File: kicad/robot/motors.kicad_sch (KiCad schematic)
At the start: 20 parts, among them J3 Conn_01x06_MountingPin, J5 Conn_01x06_MountingPin, Q6 SN74AHC125RGYR, U8 DRV8830DRCR, U9 DRV8830DRCR

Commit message: Exported all schematic symbols to local robot and refer to them in all symbols
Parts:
- C40, C41, C42, C43, C44, C74: symbol Device:C -> robot:C
- J3, J5: symbol Connector_Generic_MountingPin:Conn_01x06_MountingPin -> robot:Conn_01x06_MountingPin
- Q6: symbol ultralibrarian:SN74AHC125RGYR -> robot:SN74AHC125RGYR
- R26, R27, R28, R29, R30, R31: symbol Device:R -> robot:R
- U8, U9: symbol Driver_Motor:DRV8830DRCR -> robot:DRV8830DRCR
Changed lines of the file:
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@@
     (effects (font (size 1.27 1.27)) (justify right))
   )
-  (symbol (lib_id "ultralibrarian:SN74AHC125RGYR") (at 218.44 160.02 0) (unit 1)
+  (symbol (lib_id "robot:SN74AHC125RGYR") (at 218.44 160.02 0) (unit 1)
     (in_bom yes) (on_board yes) (dnp no) (fields_autoplaced)
     (property "Reference" "Q6" (at 221.7294 135.89 0)
@@
     )
   )
-  (symbol (lib_id "Connector_Generic_MountingPin:Conn_01x06_MountingPin") (at 245.11 52.07 0) (mirror y) (unit 1)
+  (symbol (lib_id "robot:Conn_01x06_MountingPin") (at 245.11 52.07 0) (mirror y) (unit 1)
     (in_bom yes) (on_board yes) (dnp no) (fields_autoplaced)
     (property "Reference" "J3" (at 242.57 52.4256 0)
@@
     )
   )
-  (symbol (lib_id "Device:R") (at 59.69 140.97 0) (unit 1)
+  (symbol (lib_id "robot:R") (at 59.69 140.97 0) (unit 1)
     (in_bom no) (on_board yes) (dnp yes) (fields_autoplaced)
     (property "Reference" "R27" (at 62.23 139.6999 0)
@@
     )
   )
-  (symbol (lib_id "Device:C") (at 160.02 120.65 0) (mirror y) (unit 1)
+  (symbol (lib_id "robot:C") (at 160.02 120.65 0) (mirror y) (unit 1)
     (in_bom no) (on_board yes) (dnp yes)
     (property "Reference" "C74" (at 156.21 118.1099 0)
@@
     )
   )
-  (symbol (lib_id "Device:C") (at 160.02 49.53 0) (mirror y) (unit 1)
+  (symbol (lib_id "robot:C") (at 160.02 49.53 0) (mirror y) (unit 1)
     (in_bom no) (on_board yes) (dnp yes)
     (property "Reference" "C74" (at 156.21 46.9899 0)
@@
     )
   )
-  (symbol (lib_id "Connector_Generic_MountingPin:Conn_01x06_MountingPin") (at 232.41 52.07 0) (unit 1)
+  (symbol (lib_id "robot:Conn_01x06_MountingPin") (at 232.41 52.07 0) (unit 1)
     (in_bom yes) (on_board yes) (dnp no) (fields_autoplaced)
     (property "Reference" "J5" (at 234.95 52.4256 0)
@@
     )
   )
-  (symbol (lib_id "Device:C") (at 130.81 49.53 0) (unit 1)
+  (symbol (lib_id "robot:C") (at 130.81 49.53 0) (unit 1)
     (in_bom yes) (on_board yes) (dnp no)
     (property "Reference" "C42" (at 134.62 48.2599 0)
@@
     )
   )
-  (symbol (lib_id "Device:R") (at 67.31 41.91 0) (unit 1)
+  (symbol (lib_id "robot:R") (at 67.31 41.91 0) (unit 1)
     (in_bom yes) (on_board yes) (dnp no) (fields_autoplaced)
     (property "Reference" "R28" (at 69.85 40.6399 0)
@@
     )
   )
-  (symbol (lib_id "Device:C") (at 118.11 49.53 0) (unit 1)
+  (symbol (lib_id "robot:C") (at 118.11 49.53 0) (unit 1)
     (in_bom yes) (on_board yes) (dnp no)
     (property "Reference" "C40" (at 121.92 48.2599 0)
@@
     )
   )
-  (symbol (lib_id "Device:R") (at 59.69 69.85 0) (unit 1)
+  (symbol (lib_id "robot:R") (at 59.69 69.85 0) (unit 1)
     (in_bom no) (on_board yes) (dnp yes) (fields_autoplaced)
     (property "Reference" "R26" (at 62.23 68.5799 0)
@@
     )
   )
-  (symbol (lib_id "Device:R") (at 73.66 111.76 0) (unit 1)
+  (symbol (lib_id "robot:R") (at 73.66 111.76 0) (unit 1)
     (in_bom yes) (on_board yes) (dnp no) (fields_autoplaced)
     (property "Reference" "R31" (at 76.2 110.4899 0)
@@
     )
   )
-  (symbol (lib_id "Device:R") (at 68.58 140.97 0) (unit 1)
+  (symbol (lib_id "robot:R") (at 68.58 140.97 0) (unit 1)
     (in_bom yes) (on_board yes) (dnp no) (fields_autoplaced)
     (property "Reference" "R30" (at 70.358 140.1353 0)
@@
     )
   )
-  (symbol (lib_id "Device:C") (at 148.59 120.65 0) (mirror y) (unit 1)
+  (symbol (lib_id "robot:C") (at 148.59 120.65 0) (mirror y) (unit 1)
     (in_bom no) (on_board yes) (dnp yes)
     (property "Reference" "C74" (at 144.78 118.1099 0)
@@
     )
   )
-  (symbol (lib_id "Device:C") (at 130.81 120.65 0) (unit 1)
+  (symbol (lib_id "robot:C") (at 130.81 120.65 0) (unit 1)
     (in_bom yes) (on_board yes) (dnp no)
     (property "Reference" "C43" (at 134.62 119.3799 0)
@@
     )
   )
-  (symbol (lib_id "Driver_Motor:DRV8830DRCR") (at 96.52 129.54 0) (unit 1)
+  (symbol (lib_id "robot:DRV8830DRCR") (at 96.52 129.54 0) (unit 1)
     (in_bom yes) (on_board yes) (dnp no) (fields_autoplaced)
     (property "Reference" "U9" (at 96.52 109.22 0)
@@
     )
   )
-  (symbol (lib_id "Device:C") (at 118.11 120.65 0) (unit 1)
+  (symbol (lib_id "robot:C") (at 118.11 120.65 0) (unit 1)
     (in_bom yes) (on_board yes) (dnp no)
     (property "Reference" "C41" (at 121.92 119.3799 0)
@@
     )
   )
-  (symbol (lib_id "Driver_Motor:DRV8830DRCR") (at 96.52 58.42 0) (unit 1)
+  (symbol (lib_id "robot:DRV8830DRCR") (at 96.52 58.42 0) (unit 1)
     (in_bom yes) (on_board yes) (dnp no) (fields_autoplaced)
     (property "Reference" "U8" (at 96.52 38.1 0)
@@
     )
   )
-  (symbol (lib_id "Device:C") (at 251.46 161.29 0) (unit 1)
+  (symbol (lib_id "robot:C") (at 251.46 161.29 0) (unit 1)
     (in_bom yes) (on_board yes) (dnp no)
     (property "Reference" "C44" (at 255.27 160.0199 0)
@@
     )
   )
-  (symbol (lib_id "Device:R") (at 68.58 69.85 0) (unit 1)
+  (symbol (lib_id "robot:R") (at 68.58 69.85 0) (unit 1)
     (in_bom yes) (on_board yes) (dnp no) (fields_autoplaced)
     (property "Reference" "R29" (at 70.358 69.0153 0)
@@
     )
   )
-  (symbol (lib_id "Device:C") (at 148.59 49.53 0) (mirror y) (unit 1)
+  (symbol (lib_id "robot:C") (at 148.59 49.53 0) (mirror y) (unit 1)
     (in_bom no) (on_board yes) (dnp yes)
     (property "Reference" "C74" (at 144.78 46.9899 0)

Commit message: Removing a bunch of unneccesary symbol properties
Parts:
- Q6: Stock 50 -> (none)
- U8, U9: MAXIMUM_PACKAGE_HEIGHT 1.0mm -> (none); PARTREV G -> (none); STANDARD Manufacturer Recommendations -> (none); Stock 30 -> (none)
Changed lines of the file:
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@@
-      (effects (font (size 1.27 1.27)) hide)
-    )
-    (property "Stock" "50" (at 218.44 160.02 0)
       (effects (font (size 1.27 1.27)) hide)
     )
@@
       (effects (font (size 1.27 1.27)) (justify left bottom) hide)
     )
-    (property "MAXIMUM_PACKAGE_HEIGHT" "1.0mm" (at 83.82 157.48 0)
-      (effects (font (size 1.27 1.27)) (justify left bottom) hide)
-    )
-    (property "STANDARD" "Manufacturer Recommendations" (at 83.82 154.94 0)
-      (effects (font (size 1.27 1.27)) (justify left bottom) hide)
-    )
-    (property "MANUFACTURER" "" (at 83.82 152.4 0)
-      (effects (font (size 1.27 1.27)) (justify left bottom) hide)
-    )
-    (property "PARTREV" "G" (at 83.82 160.02 0)
-      (effects (font (size 1.27 1.27)) (justify left bottom) hide)
-    )
     (property "Description" "Provide adequate heat sinking on PCB" (at 96.52 129.54 0)
       (effects (font (size 1.27 1.27)) hide)
@@
     )
     (property "Part Number" "DRV8830DRCR" (at 96.52 129.54 0)
-      (effects (font (size 1.27 1.27)) hide)
-    )
-    (property "Stock" "30" (at 96.52 129.54 0)
       (effects (font (size 1.27 1.27)) hide)
     )
@@
       (effects (font (size 1.27 1.27)) (justify left bottom) hide)
     )
-    (property "MAXIMUM_PACKAGE_HEIGHT" "1.0mm" (at 83.82 86.36 0)
-      (effects (font (size 1.27 1.27)) (justify left bottom) hide)
-    )
-    (property "STANDARD" "Manufacturer Recommendations" (at 83.82 83.82 0)
-      (effects (font (size 1.27 1.27)) (justify left bottom) hide)
-    )
-    (property "MANUFACTURER" "" (at 83.82 81.28 0)
-      (effects (font (size 1.27 1.27)) (justify left bottom) hide)
-    )
-    (property "PARTREV" "G" (at 83.82 88.9 0)
-      (effects (font (size 1.27 1.27)) (justify left bottom) hide)
-    )
     (property "Description" "Provide adequate heat sinking on PCB" (at 96.52 58.42 0)
       (effects (font (size 1.27 1.27)) hide)
@@
       (effects (font (size 1.27 1.27)) hide)
     )
-    (property "Stock" "30" (at 96.52 58.42 0)
-      (effects (font (size 1.27 1.27)) hide)
-    )

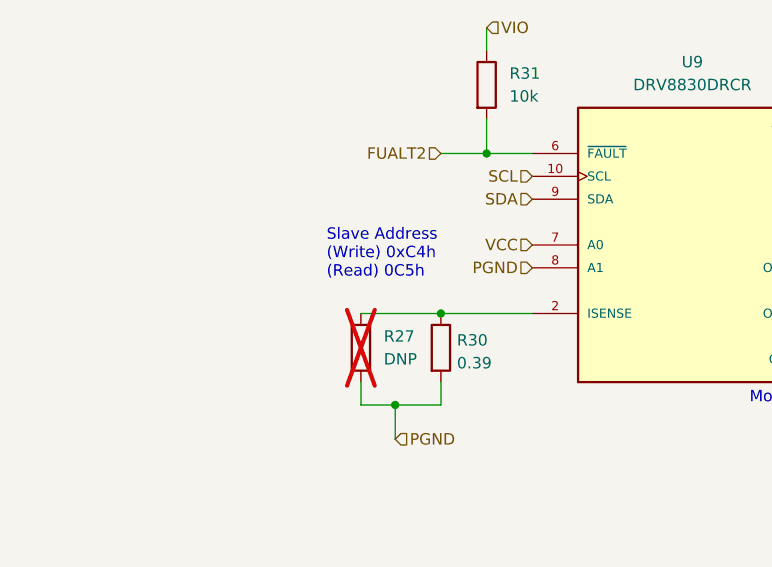
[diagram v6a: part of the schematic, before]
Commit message: Added power_2A net classes and net ties to schematic
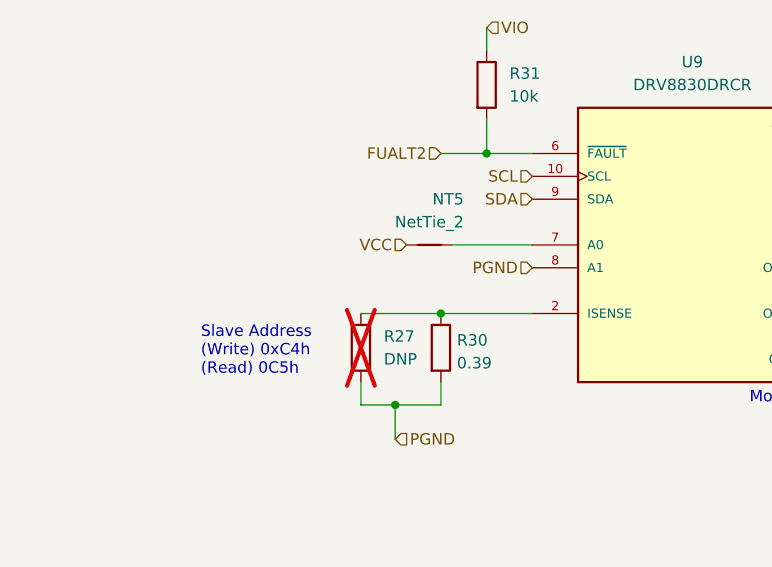
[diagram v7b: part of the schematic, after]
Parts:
- added NT5: NetTie_2, robot:NetTie-_SMD_Pad6mil, symbol Device:NetTie_2
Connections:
- net VCC: now also NT5.2; no longer U9.7 (A0)
- new net: NT5.1, U9.7 (A0)
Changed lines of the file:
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@@
+    (stroke (width 0) (type default))
+  )
+  (wire (pts (xy 69.85 129.54) (xy 78.74 129.54))
     (stroke (width 0) (type default))
   )
@@
     (effects (font (size 1.27 1.27)) (justify left bottom))
   )
-  (text "Slave Address \n(Write) 0xC4h \n(Read) 0C5h" (at 55.88 133.35 0)
+  (text "Slave Address \n(Write) 0xC4h \n(Read) 0C5h" (at 41.91 144.145 0)
     (effects (font (size 1.27 1.27)) (justify left bottom))
   )
@@
     (effects (font (size 1.27 1.27)) (justify left))
   )
-  (hierarchical_label "VCC" (shape input) (at 78.74 129.54 180) (fields_autoplaced)
+  (hierarchical_label "VCC" (shape input) (at 64.77 129.54 180) (fields_autoplaced)
     (effects (font (size 1.27 1.27)) (justify right))
   )
@@
   (hierarchical_label "PGND" (shape input) (at 78.74 132.08 180) (fields_autoplaced)
     (effects (font (size 1.27 1.27)) (justify right))
+  )
+  (netclass_flag "" (length 2.54) (shape round) (at 115.57 66.04 0) (fields_autoplaced)
+    (effects (font (size 1.27 1.27)) (justify left bottom))
+    (property "Netclass" "power_2A" (at 116.2685 63.5 0)
+      (effects (font (size 1.27 1.27) italic) (justify left) hide)
+    )
+  )
+  (netclass_flag "" (length 2.54) (shape round) (at 115.57 60.96 0) (fields_autoplaced)
+    (effects (font (size 1.27 1.27)) (justify left bottom))
+    (property "Netclass" "power_2A" (at 116.2685 58.42 0)
+      (effects (font (size 1.27 1.27) italic) (justify left) hide)
+    )
+  )
+  (netclass_flag "" (length 2.54) (shape round) (at 114.935 132.08 0) (fields_autoplaced)
+    (effects (font (size 1.27 1.27)) (justify left bottom))
+    (property "Netclass" "power_2A" (at 115.6335 129.54 0)
+      (effects (font (size 1.27 1.27) italic) (justify left) hide)
+    )
+  )
+  (netclass_flag "" (length 2.54) (shape round) (at 114.935 137.16 0) (fields_autoplaced)
+    (effects (font (size 1.27 1.27)) (justify left bottom))
+    (property "Netclass" "power_2A" (at 115.6335 134.62 0)
+      (effects (font (size 1.27 1.27) italic) (justify left) hide)
+    )
   )
   (symbol (lib_id "robot:SN74AHC125RGYR") (at 218.44 160.02 0) (unit 1)
@@
         )
       )
+    )
+  )
+  (symbol (lib_id "Device:NetTie_2") (at 67.31 129.54 0) (mirror y) (unit 1)
+    (in_bom no) (on_board yes) (dnp no)
+    (property "Reference" "NT5" (at 71.12 124.46 0)
+      (effects (font (size 1.27 1.27)) (justify left))
+    )
+    (property "Value" "NetTie_2" (at 71.12 127 0)
+      (effects (font (size 1.27 1.27)) (justify left))
+    )
+    (property "Footprint" "robot:NetTie-_SMD_Pad6mil" (at 67.31 129.54 0)
+      (effects (font (size 1.27 1.27)) hide)
+    )
+    (property "Datasheet" "~" (at 67.31 129.54 0)
+      (effects (font (size 1.27 1.27)) hide)
+    )
+    (pin "1")
+    (pin "2")
+    (instances
+      (project "robot"
+        (path "/0c7b298e-2d07-4b1f-b033-e95f02d45089/3fab603d-ed65-41bd-8de1-51639e39cb06"
+          (reference "NT5") (unit 1)
+        )
+        (path "/0c7b298e-2d07-4b1f-b033-e95f02d45089/aaf20b87-68dc-43c9-a7d3-4ceda8b87424"
+          (reference "NT15") (unit 1)
+        )
+        (path "/0c7b298e-2d07-4b1f-b033-e95f02d45089/427922e5-a943-4728-8788-709c0c3b2395"
+          (reference "NT16") (unit 1)
+        )
+        (path "/0c7b298e-2d07-4b1f-b033-e95f02d45089/4bf796fd-fdb4-45d1-808a-a634d5f4571e"
+          (reference "NT17") (unit 1)
+        )
+      )

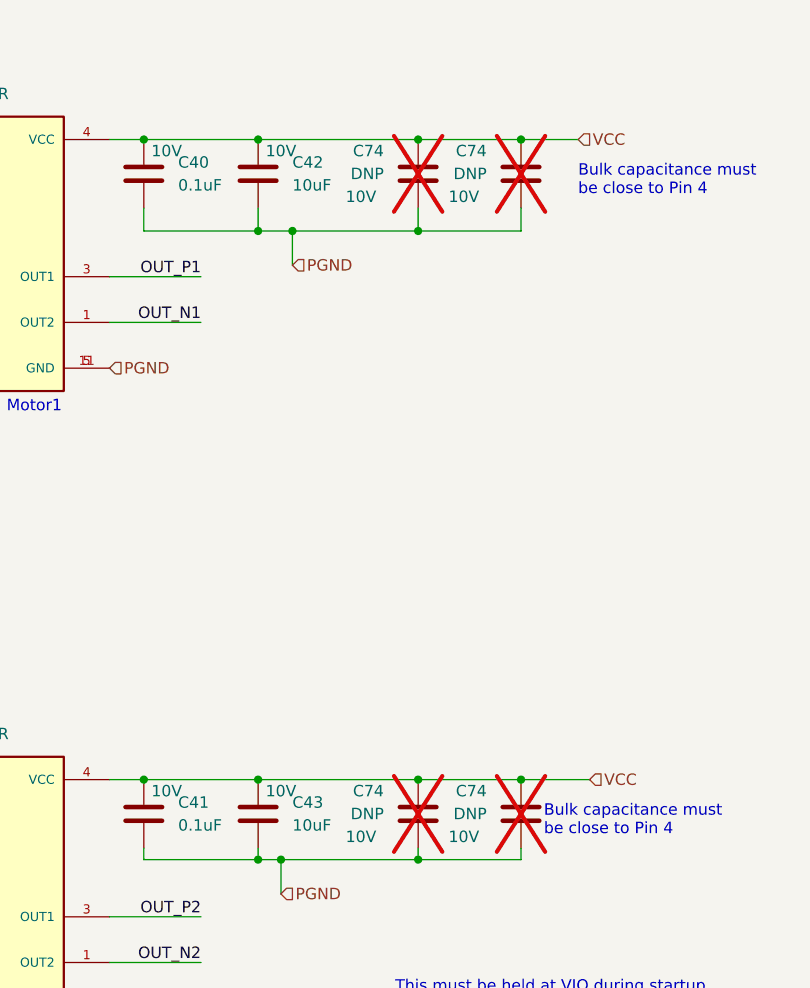
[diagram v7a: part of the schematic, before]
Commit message: Updating symbol fields for BOM completion.
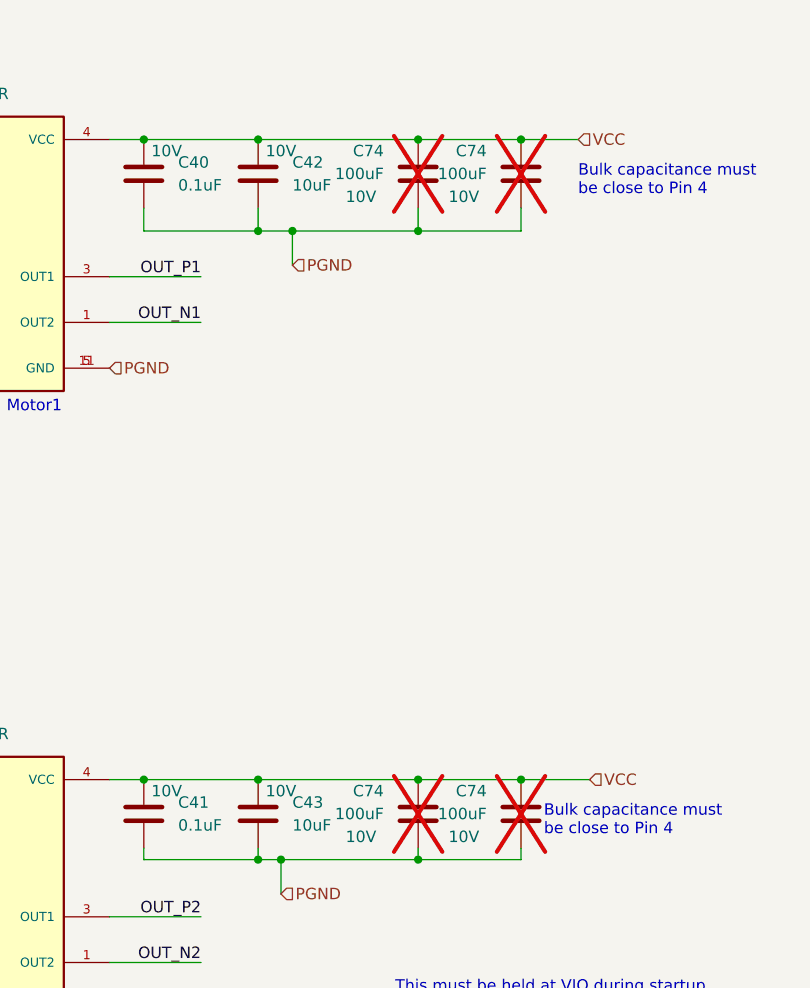
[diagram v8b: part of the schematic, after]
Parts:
- C74: value DNP -> 100uF; Manufacturer DNP -> Murata; Part Number DNP -> GRM31CD80J107MEA8K
- J3, J5: Manufacturer (none) -> JST; Part Number (none) -> B6B-ZR-SM4-TF
- NT5: Manufacturer (none) -> N/A; Part Number (none) -> N/A
- R26, R27: Manufacturer DNP -> Panasonic; Part Number DNP -> ERJ-3RQJR39V
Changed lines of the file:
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@@
+      (effects (font (size 1.27 1.27)) hide)
+    )
+    (property "Manufacturer" "N/A" (at 67.31 129.54 0)
+      (effects (font (size 1.27 1.27)) hide)
+    )
+    (property "Part Number" "N/A" (at 67.31 129.54 0)
       (effects (font (size 1.27 1.27)) hide)
     )
@@
     )
     (property "Datasheet" "https://www.jst-mfg.com/product/pdf/eng/eZH.pdf" (at 245.11 52.07 0)
+      (effects (font (size 1.27 1.27)) hide)
+    )
+    (property "Manufacturer" "JST" (at 245.11 52.07 0)
+      (effects (font (size 1.27 1.27)) hide)
+    )
+    (property "Part Number" "B6B-ZR-SM4-TF" (at 245.11 52.07 0)
       (effects (font (size 1.27 1.27)) hide)
     )
@@
       (effects (font (size 1.27 1.27)) hide)
     )
-    (property "Manufacturer" "DNP" (at 59.69 140.97 0)
-      (effects (font (size 1.27 1.27)) hide)
-    )
-    (property "Part Number" "DNP" (at 59.69 140.97 0)
+    (property "Manufacturer" "Panasonic" (at 59.69 140.97 0)
+      (effects (font (size 1.27 1.27)) hide)
+    )
+    (property "Part Number" "ERJ-3RQJR39V" (at 59.69 140.97 0)
       (effects (font (size 1.27 1.27)) hide)
     )
@@
       (effects (font (size 1.27 1.27)) (justify left))
     )
-    (property "Value" "DNP" (at 156.21 120.6499 0)
+    (property "Value" "100uF" (at 156.21 120.6499 0)
       (effects (font (size 1.27 1.27)) (justify left))
     )
@@
       (effects (font (size 1.27 1.27)))
     )
-    (property "Manufacturer" "DNP" (at 160.02 120.65 0)
-      (effects (font (size 1.27 1.27)) hide)
-    )
-    (property "Part Number" "DNP" (at 160.02 120.65 0)
+    (property "Manufacturer" "Murata" (at 160.02 120.65 0)
+      (effects (font (size 1.27 1.27)) hide)
+    )
+    (property "Part Number" "GRM31CD80J107MEA8K" (at 160.02 120.65 0)
       (effects (font (size 1.27 1.27)) hide)
     )
@@
       (effects (font (size 1.27 1.27)) (justify left))
     )
-    (property "Value" "DNP" (at 156.21 49.5299 0)
+    (property "Value" "100uF" (at 156.21 49.5299 0)
       (effects (font (size 1.27 1.27)) (justify left))
     )
@@
       (effects (font (size 1.27 1.27)))
     )
-    (property "Manufacturer" "DNP" (at 160.02 49.53 0)
-      (effects (font (size 1.27 1.27)) hide)
-    )
-    (property "Part Number" "DNP" (at 160.02 49.53 0)
+    (property "Manufacturer" "Murata" (at 160.02 49.53 0)
+      (effects (font (size 1.27 1.27)) hide)
+    )
+    (property "Part Number" "GRM31CD80J107MEA8K" (at 160.02 49.53 0)
       (effects (font (size 1.27 1.27)) hide)
     )
@@
     )
     (property "Datasheet" "https://www.jst-mfg.com/product/pdf/eng/eZH.pdf" (at 232.41 52.07 0)
+      (effects (font (size 1.27 1.27)) hide)
+    )
+    (property "Manufacturer" "JST" (at 232.41 52.07 0)
+      (effects (font (size 1.27 1.27)) hide)
+    )
+    (property "Part Number" "B6B-ZR-SM4-TF" (at 232.41 52.07 0)
       (effects (font (size 1.27 1.27)) hide)
     )
@@
       (effects (font (size 1.27 1.27)) hide)
     )
-    (property "Manufacturer" "DNP" (at 59.69 69.85 0)
-      (effects (font (size 1.27 1.27)) hide)
-    )
-    (property "Part Number" "DNP" (at 59.69 69.85 0)
+    (property "Manufacturer" "Panasonic" (at 59.69 69.85 0)
+      (effects (font (size 1.27 1.27)) hide)
+    )
+    (property "Part Number" "ERJ-3RQJR39V" (at 59.69 69.85 0)
       (effects (font (size 1.27 1.27)) hide)
     )
@@
       (effects (font (size 1.27 1.27)) (justify left))
     )
-    (property "Value" "DNP" (at 144.78 120.6499 0)
+    (property "Value" "100uF" (at 144.78 120.6499 0)
       (effects (font (size 1.27 1.27)) (justify left))
     )
@@
       (effects (font (size 1.27 1.27)))
     )
-    (property "Manufacturer" "DNP" (at 148.59 120.65 0)
-      (effects (font (size 1.27 1.27)) hide)
-    )
-    (property "Part Number" "DNP" (at 148.59 120.65 0)
+    (property "Manufacturer" "Murata" (at 148.59 120.65 0)
+      (effects (font (size 1.27 1.27)) hide)
+    )
+    (property "Part Number" "GRM31CD80J107MEA8K" (at 148.59 120.65 0)
       (effects (font (size 1.27 1.27)) hide)
     )
@@
       (effects (font (size 1.27 1.27)) (justify left))
     )
-    (property "Value" "DNP" (at 144.78 49.5299 0)
+    (property "Value" "100uF" (at 144.78 49.5299 0)
       (effects (font (size 1.27 1.27)) (justify left))
     )
@@
       (effects (font (size 1.27 1.27)))
     )
-    (property "Manufacturer" "DNP" (at 148.59 49.53 0)
-      (effects (font (size 1.27 1.27)) hide)
-    )
-    (property "Part Number" "DNP" (at 148.59 49.53 0)
-      (effects (font (size 1.27 1.27)) hide)
-    )
+    (property "Manufacturer" "Murata" (at 148.59 49.53 0)
+      (effects (font (size 1.27 1.27)) hide)
+    )
+    (property "Part Number" "GRM31CD80J107MEA8K" (at 148.59 49.53 0)
+      (effects (font (size 1.27 1.27)) hide)
+    )
